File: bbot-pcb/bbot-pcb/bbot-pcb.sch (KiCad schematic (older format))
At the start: 9 parts, among them U1 HA-552-4P, U10 L293D, U2 HMC5883L, U3 HA-552-4P, U4 ArduinoProMicro, U5 L7805, U6 Screw_Terminal_2, U7 74HC595, U9 L293D

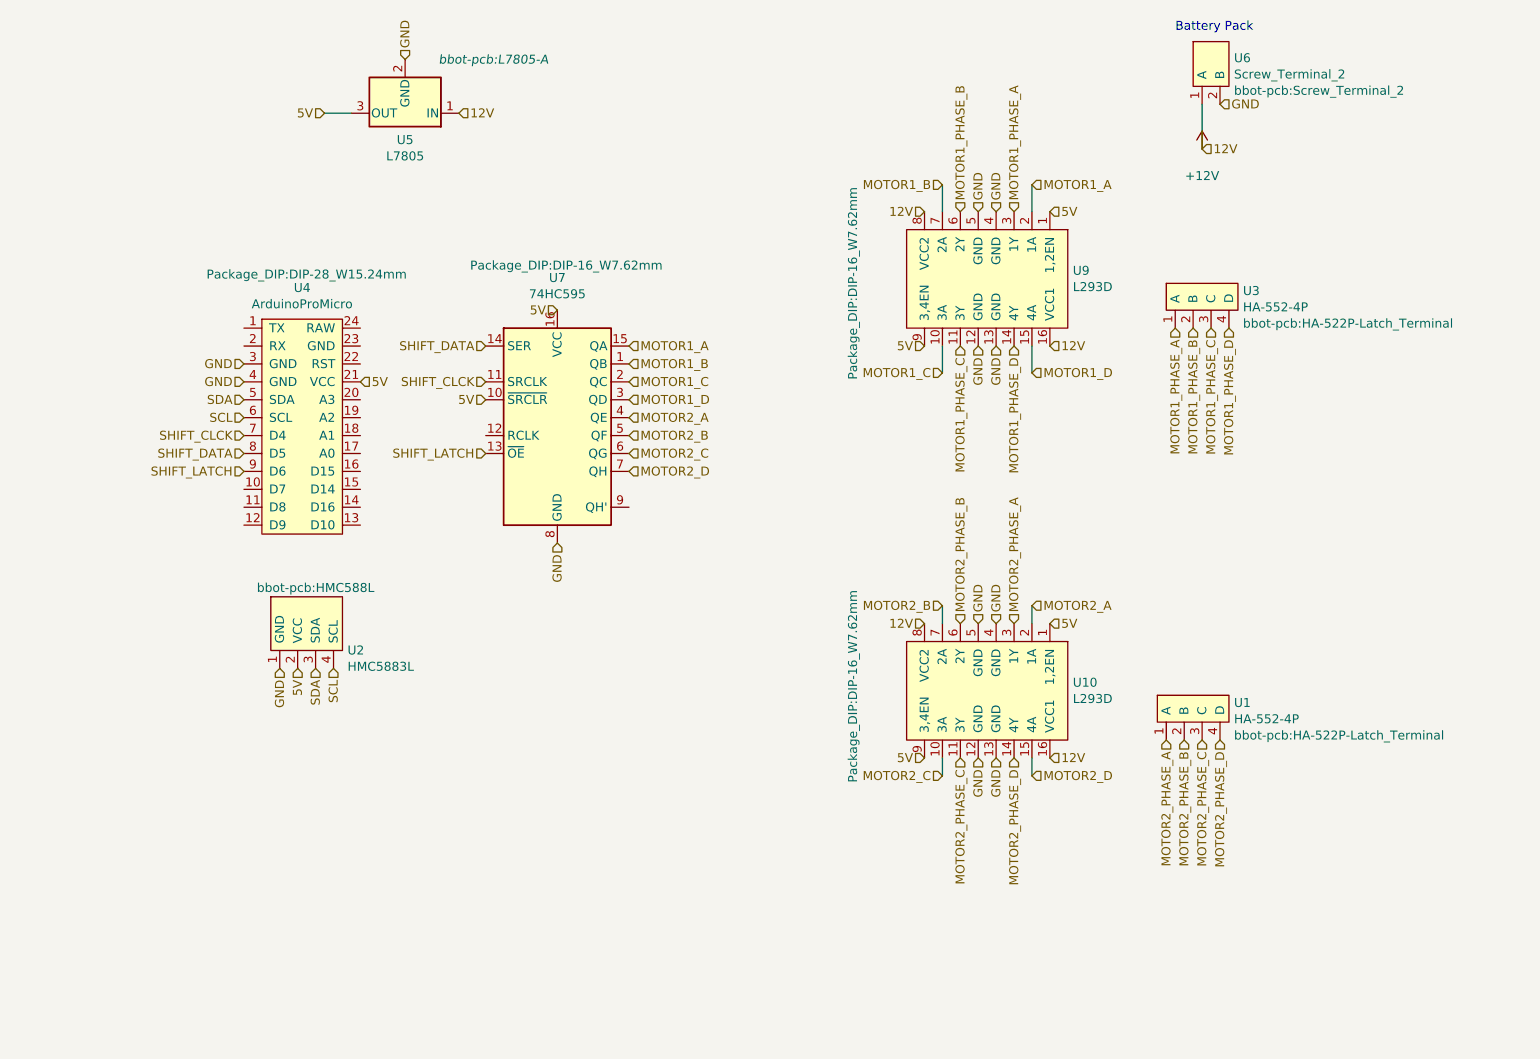
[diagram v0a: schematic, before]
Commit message: unverified prototype of completed circuit board design. not quite ready to ship off to a fab yet
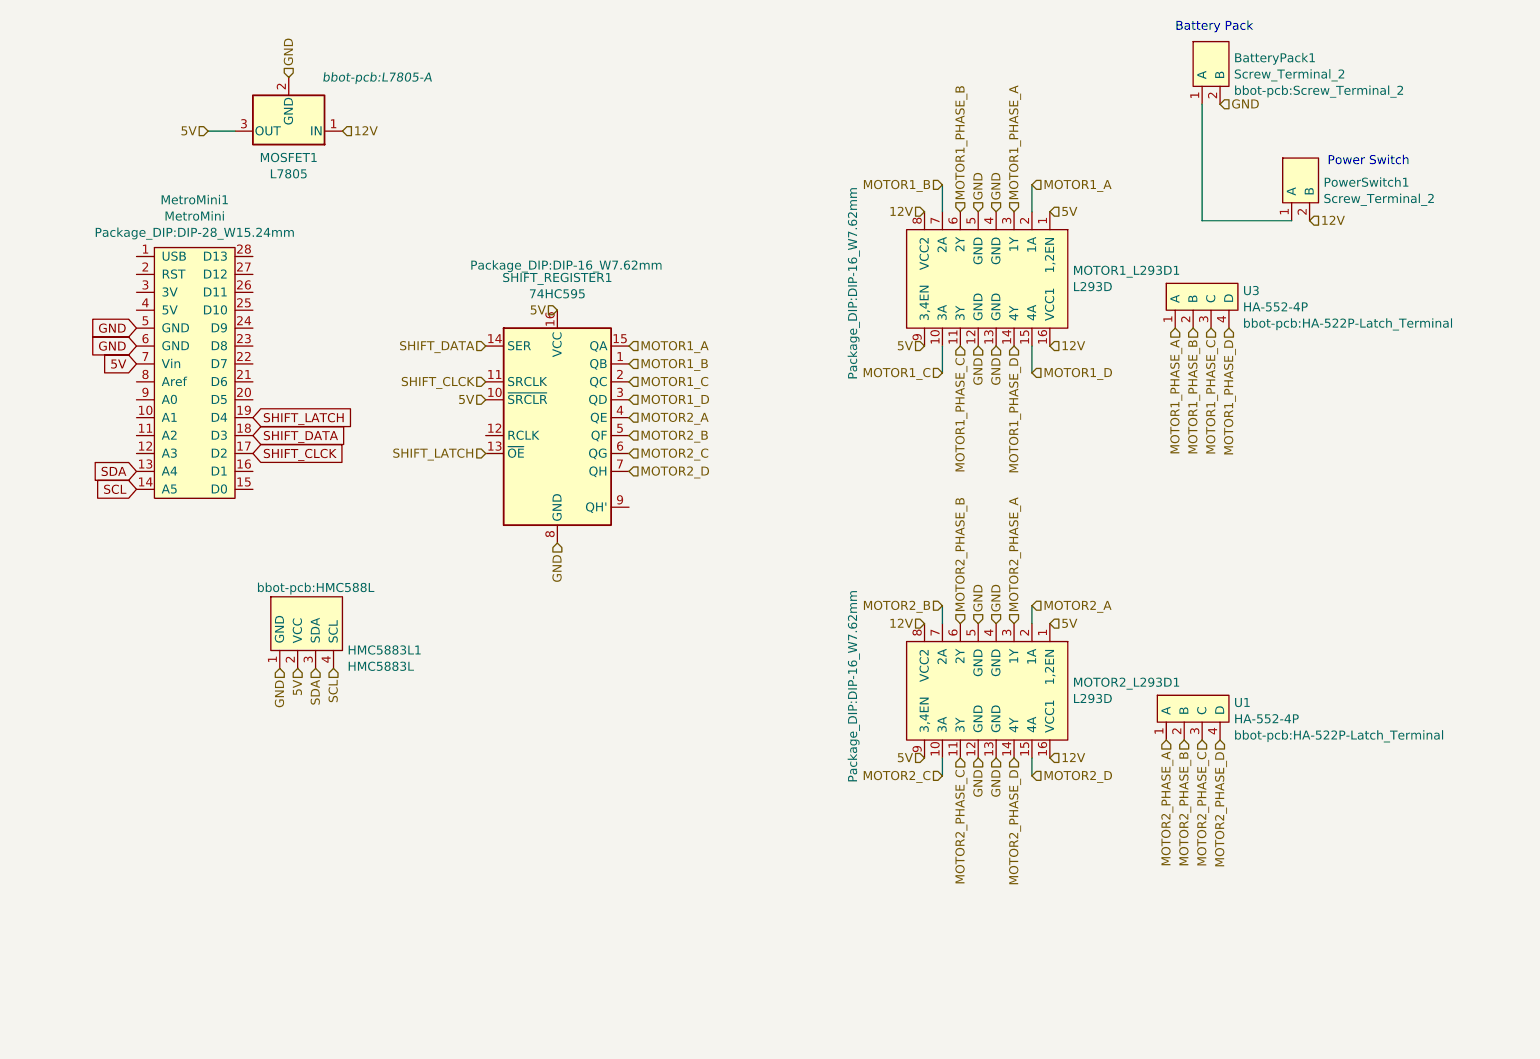
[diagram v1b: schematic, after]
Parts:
- removed U4: ArduinoProMicro, Package_DIP:DIP-28_W15.24mm, symbol bbot-component-library:ArduinoProMicro
- added MetroMini1: MetroMini, Package_DIP:DIP-28_W15.24mm, symbol bbot-component-library:MetroMini
- added PowerSwitch1: Screw_Terminal_2, bbot-pcb:Screw_Terminal_2, symbol bbot-component-library:Screw_Terminal_2
- renumbered U6 to BatteryPack1, U2 to HMC5883L1, U5 to MOSFET1, U9 to MOTOR1_L293D1, U10 to MOTOR2_L293D1, U7 to SHIFT_REGISTER1
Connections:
- net 5V: now also MetroMini1.7 (Vin)
- net GND: now also MetroMini1.5 (GND), MetroMini1.6 (GND)
- net SCL: now also MetroMini1.14 (A5)
- net SDA: now also MetroMini1.13 (A4)
- net SHIFT_CLCK: now also MetroMini1.17 (D2)
- net SHIFT_DATA: now also MetroMini1.18 (D3)
- net SHIFT_LATCH: now also MetroMini1.19 (D4)
- net +12V renamed 12V
- net 12V: now also PowerSwitch1.2 (B); no longer BatteryPack1.1 (A)
- new net: BatteryPack1.1 (A), PowerSwitch1.1 (A)
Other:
- note added: "Power Switch"
- moved on the sheet: MOSFET1
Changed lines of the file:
@@
 $EndDescr
 $Comp
-L bbot-component-library:L293D U9
+L bbot-component-library:L293D MOTOR1_L293D1
 U 1 1 606C2560
 P 5950 2000
-F 0 "U9" V 5879 2478 50  0000 L CNN
+F 0 "MOTOR1_L293D1" V 5879 2478 50  0000 L CNN
 F 1 "L293D" V 5970 2478 50  0000 L CNN
 F 2 "Package_DIP:DIP-16_W7.62mm" H 5950 1250 50  0000 C CNN
@@
 $EndComp
 $Comp
-L Regulator_Linear:L7805 U5
-U 1 1 606D0E09
-P 2700 1050
-F 0 "U5" H 2700 1199 50  0000 C CNN
-F 1 "L7805" H 2700 1290 50  0000 C CNN
-F 2 "bbot-pcb:L7805-A" H 1900 750 50  0000 L CIN
-F 3 "http://www.st.com/content/ccc/resource/technical/document/datasheet/41/4f/b3/b0/12/d4/47/88/CD00000444.pdf/files/CD00000444.pdf/jcr:content/translations/en.CD00000444.pdf" H 2700 1000 50  0001 C CNN
-	1    2700 1050
-	-1   0    0    1
-$EndComp
-$Comp
-L bbot-component-library:ArduinoProMicro U4
-U 1 1 606D85DE
-P 2200 2750
-F 0 "U4" H 2125 3475 50  0000 C CNN
-F 1 "ArduinoProMicro" H 2125 3384 50  0000 C CNN
-F 2 "Package_DIP:DIP-28_W15.24mm" H 2150 3550 50  0000 C CNN
-F 3 "" H 1900 3550 50  0001 C CNN
-	1    2200 2750
-	1    0    0    -1
-$EndComp
-$Comp
-L power:+12V #PWR0101
-U 1 1 606DFC80
-P 7150 1250
-F 0 "#PWR0101" H 7150 1100 50  0001 C CNN
-F 1 "+12V" H 7150 1100 50  0000 C CNN
-F 2 "" H 7150 1250 50  0001 C CNN
-F 3 "" H 7150 1250 50  0001 C CNN
-	1    7150 1250
-	1    0    0    -1
-$EndComp
-$Comp
-L 74xx:74HC595 U7
+L 74xx:74HC595 SHIFT_REGISTER1
 U 1 1 606C82E5
 P 3550 2750
-F 0 "U7" H 3550 3531 50  0000 C CNN
+F 0 "SHIFT_REGISTER1" H 3550 3531 50  0000 C CNN
 F 1 "74HC595" H 3550 3440 50  0000 C CNN
 F 2 "Package_DIP:DIP-16_W7.62mm" H 3600 3600 50  0000 C CNN
@@
 Text HLabel 2000 4150 3    50   Input ~ 0
 GND
-Text HLabel 1800 2450 0    50   Input ~ 0
-GND
-Text HLabel 1800 2550 0    50   Input ~ 0
-GND
-Text HLabel 2700 750  1    50   Input ~ 0
-GND
-Text HLabel 7150 1250 2    50   Input ~ 0
-12V
-Text HLabel 3000 1050 2    50   Input ~ 0
+Text HLabel 2050 850  1    50   Input ~ 0
+GND
+Text HLabel 2350 1150 2    50   Input ~ 0
 12V
 Text HLabel 6300 2350 2    50   Input ~ 0
@@
 12V
 Wire Wire Line
-	2400 1050 2250 1050
-Text HLabel 2250 1050 0    50   Input ~ 0
-5V
-Text HLabel 2450 2550 2    50   Input ~ 0
+	1750 1150 1600 1150
+Text HLabel 1600 1150 0    50   Input ~ 0
 5V
 Text HLabel 3550 2150 0    50   Input ~ 0
@@
 SDA
 Text HLabel 2300 4150 3    50   Input ~ 0
-SCL
-Text HLabel 1800 2650 0    50   Input ~ 0
-SDA
-Text HLabel 1800 2750 0    50   Input ~ 0
 SCL
 Text HLabel 6100 1600 1    50   Input ~ 0
@@
 MOTOR1_PHASE_D
 $Comp
-L bbot-component-library:L293D U10
+L bbot-component-library:L293D MOTOR2_L293D1
 U 1 1 606C1081
 P 5950 4300
-F 0 "U10" V 5879 4778 50  0000 L CNN
+F 0 "MOTOR2_L293D1" V 5879 4778 50  0000 L CNN
 F 1 "L293D" V 5970 4778 50  0000 L CNN
 F 2 "Package_DIP:DIP-16_W7.62mm" H 5900 3550 50  0000 C CNN
@@
 Text HLabel 3150 2350 0    50   Input ~ 0
 SHIFT_DATA
-Text HLabel 1800 2850 0    50   Input ~ 0
-SHIFT_CLCK
-Text HLabel 1800 2950 0    50   Input ~ 0
-SHIFT_DATA
-Text HLabel 1800 3050 0    50   Input ~ 0
-SHIFT_LATCH
 $Comp
 L bbot-component-library:HA-552-4P U1
@@
 MOTOR2_PHASE_A
 $Comp
-L bbot-component-library:HMC5883L U2
+L bbot-component-library:HMC5883L HMC5883L1
 U 1 1 606D2B12
 P 2150 4000
-F 0 "U2" H 2378 3951 50  0000 L CNN
+F 0 "HMC5883L1" H 2378 3951 50  0000 L CNN
 F 1 "HMC5883L" H 2378 3860 50  0000 L CNN
 F 2 "bbot-pcb:HMC588L" H 2200 4300 50  0000 C CNN
@@
 $EndComp
 $Comp
-L bbot-component-library:Screw_Terminal_2 U6
+L bbot-component-library:Screw_Terminal_2 BatteryPack1
 U 1 1 607194F6
 P 7150 1000
-F 0 "U6" H 7328 1258 50  0000 L CNN
+F 0 "BatteryPack1" H 7328 1258 50  0000 L CNN
 F 1 "Screw_Terminal_2" H 7328 1167 50  0000 L CNN
 F 2 "bbot-pcb:Screw_Terminal_2" H 7328 1076 50  0000 L CNN
@@
 Text Notes 7000 600  0    50   ~ 0
 Battery Pack
-Wire Wire Line
-	7150 1250 7150 1000
 Text HLabel 7250 1000 2    50   Input ~ 0
 GND
+$Comp
+L Regulator_Linear:L7805 MOSFET1
+U 1 1 606D0E09
+P 2050 1150
+F 0 "MOSFET1" H 2050 1299 50  0000 C CNN
+F 1 "L7805" H 2050 1390 50  0000 C CNN
+F 2 "bbot-pcb:L7805-A" H 1250 850 50  0000 L CIN
+F 3 "http://www.st.com/content/ccc/resource/technical/document/datasheet/41/4f/b3/b0/12/d4/47/88/CD00000444.pdf/files/CD00000444.pdf/jcr:content/translations/en.CD00000444.pdf" H 2050 1100 50  0001 C CNN
+	1    2050 1150
+	-1   0    0    1
+$EndComp
+$Comp
+L bbot-component-library:Screw_Terminal_2 PowerSwitch1
+U 1 1 60720FFC
+P 7650 1650
+F 0 "PowerSwitch1" H 7828 1863 50  0000 L CNN
+F 1 "Screw_Terminal_2" H 7828 1772 50  0000 L CNN
+F 2 "bbot-pcb:Screw_Terminal_2" H 7650 1650 50  0001 C CNN
+F 3 "" H 7650 1650 50  0001 C CNN
+	1    7650 1650
+	1    0    0    -1
+$EndComp
+Text HLabel 7750 1650 2    50   Input ~ 0
+12V
+Text Notes 7850 1350 0    50   ~ 0
+Power Switch
+Wire Wire Line
+	7150 1000 7150 1650
+Wire Wire Line
+	7150 1650 7650 1650
+$Comp
+L bbot-component-library:MetroMini MetroMini1
+U 1 1 6072CA85
+P 1550 2500
+F 0 "MetroMini1" H 1525 3465 50  0000 C CNN
+F 1 "MetroMini" H 1525 3374 50  0000 C CNN
+F 2 "Package_DIP:DIP-28_W15.24mm" H 1525 3283 50  0000 C CNN
+F 3 "" H 1300 2850 50  0001 C CNN
+	1    1550 2500
+	1    0    0    -1
+$EndComp
+Text GLabel 1200 2450 0    50   Input ~ 0
+5V
+Text GLabel 1850 2950 2    50   Input ~ 0
+SHIFT_CLCK
+Text GLabel 1850 2850 2    50   Input ~ 0
+SHIFT_DATA
+Text GLabel 1850 2750 2    50   Input ~ 0
+SHIFT_LATCH
+Text GLabel 1200 2250 0    50   Input ~ 0
+GND
+Text GLabel 1200 2350 0    50   Input ~ 0
+GND
+Text GLabel 1200 3050 0    50   Input ~ 0
+SDA
+Text GLabel 1200 3150 0    50   Input ~ 0
+SCL
 $EndSCHEMATC

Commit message: finalize kicad circuit board.
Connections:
- net GND: now also SHIFT_REGISTER1.13 (~OE); no longer MOTOR1_L293D1.12 (GND), MOTOR1_L293D1.13 (GND), MOTOR1_L293D1.4 (GND), MOTOR2_L293D1.13 (GND), MOTOR2_L293D1.4 (GND), MOTOR2_L293D1.5 (GND)
- net SHIFT_LATCH: now also SHIFT_REGISTER1.12 (RCLK); no longer SHIFT_REGISTER1.13 (~OE)
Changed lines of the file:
@@
 Wire Wire Line
 	5700 1600 5700 1450
-Wire Wire Line
-	5700 2350 5700 2500
-Wire Wire Line
-	6200 2350 6200 2500
 Text HLabel 5700 2500 0    50   Input ~ 0
 MOTOR1_C
@@
 Text HLabel 3950 3050 2    50   Input ~ 0
 MOTOR2_D
-Text HLabel 5900 3900 1    50   Input ~ 0
-GND
-Text HLabel 6000 3900 1    50   Input ~ 0
-GND
 Text HLabel 5900 4650 3    50   Input ~ 0
 GND
-Text HLabel 6000 4650 3    50   Input ~ 0
-GND
-Text HLabel 6000 2350 3    50   Input ~ 0
-GND
-Text HLabel 5900 2350 3    50   Input ~ 0
-GND
 Text HLabel 5900 1600 1    50   Input ~ 0
-GND
-Text HLabel 6000 1600 1    50   Input ~ 0
 GND
 Text HLabel 3550 3450 3    50   Input ~ 0
@@
 5V
 Text HLabel 3150 2950 0    50   Input ~ 0
-SHIFT_LATCH
+GND
 Text HLabel 3150 2350 0    50   Input ~ 0
 SHIFT_DATA
@@
 Text GLabel 1200 3150 0    50   Input ~ 0
 SCL
+Wire Wire Line
+	5700 2350 5700 2500
+Wire Wire Line
+	6200 2350 6200 2500
+Text HLabel 3150 2850 0    50   Input ~ 0
+SHIFT_LATCH
 $EndSCHEMATC

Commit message: pcb v2 updates
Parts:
- removed HMC5883L1: HMC5883L, bbot-pcb:HMC588L, symbol bbot-component-library:HMC5883L
- added U2: ADXL335, bbot-pcb:ADXL335, symbol bbot-component-library:ADXL335
- added U4: OPENLOG, bbot-pcb:OPENLOG, symbol bbot-component-library:OPENLOG
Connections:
- net GND: now also U2.5 (GND), U4.1 (BLK), U4.2 (GND)
- net A1: now reaches MetroMini1.10 (A1)
- net A1: now also U2.3 (YOUT)
- net A2: now reaches MetroMini1.11 (A2)
- net A2: now also U2.4 (ZOUT)
- net RST: now reaches MetroMini1.2 (RST)
- net RST: now also U4.6 (GRN)
- net RX: now reaches MetroMini1.24 (D9)
- net RX: now also U4.5 (RX1)
- net TX: now reaches MetroMini1.25 (D10)
- net TX: now also U4.4 (TX0)
- net 3V: now reaches MetroMini1.3 (3V)
- net 3V: now also U2.1 (VCC), U4.3 (VCC)
- net A0: now reaches MetroMini1.9 (A0)
- net A0: now also U2.2 (XOUT)
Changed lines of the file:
@@
 Text HLabel 3550 3450 3    50   Input ~ 0
-GND
-Text HLabel 2000 4150 3    50   Input ~ 0
 GND
 Text HLabel 2050 850  1    50   Input ~ 0
@@
 Text HLabel 3550 2150 0    50   Input ~ 0
 5V
-Text HLabel 2100 4150 3    50   Input ~ 0
-5V
-Text HLabel 2200 4150 3    50   Input ~ 0
-SDA
-Text HLabel 2300 4150 3    50   Input ~ 0
-SCL
 Text HLabel 6100 1600 1    50   Input ~ 0
 MOTOR1_PHASE_A
@@
 MOTOR2_PHASE_A
 $Comp
-L bbot-component-library:HMC5883L HMC5883L1
-U 1 1 606D2B12
-P 2150 4000
-F 0 "HMC5883L1" H 2378 3951 50  0000 L CNN
-F 1 "HMC5883L" H 2378 3860 50  0000 L CNN
-F 2 "bbot-pcb:HMC588L" H 2200 4300 50  0000 C CNN
-F 3 "" H 2200 4200 50  0001 C CNN
-	1    2150 4000
-	1    0    0    -1
-$EndComp
-$Comp
 L bbot-component-library:Screw_Terminal_2 BatteryPack1
 U 1 1 607194F6
@@
 Text HLabel 3150 2850 0    50   Input ~ 0
 SHIFT_LATCH
+$Comp
+L bbot-component-library:ADXL335 U2
+U 1 1 607BD863
+P 1500 3950
+F 0 "U2" H 1778 3846 50  0000 L CNN
+F 1 "ADXL335" H 1778 3755 50  0000 L CNN
+F 2 "bbot-pcb:ADXL335" H 1550 4150 50  0000 C CNN
+F 3 "" H 1250 4000 50  0001 C CNN
+	1    1500 3950
+	1    0    0    -1
+$EndComp
+Text HLabel 1250 3900 0    50   Input ~ 0
+3V
+Text HLabel 1250 4000 0    50   Input ~ 0
+A0
+Text HLabel 1250 4100 0    50   Input ~ 0
+A1
+Text HLabel 1250 4200 0    50   Input ~ 0
+A2
+Text HLabel 1250 4300 0    50   Input ~ 0
+GND
+Text HLabel 1200 2650 0    50   Input ~ 0
+A0
+Text HLabel 1200 2750 0    50   Input ~ 0
+A1
+Text HLabel 1200 2850 0    50   Input ~ 0
+A2
+Text HLabel 1200 2050 0    50   Input ~ 0
+3V
+$Comp
+L bbot-component-library:OPENLOG U4
+U 1 1 607C091B
+P 3550 4050
+F 0 "U4" H 3828 4096 50  0000 L CNN
+F 1 "OPENLOG" H 3828 4005 50  0000 L CNN
+F 2 "bbot-pcb:OPENLOG" H 3828 3914 50  0000 L CNN
+F 3 "" H 3250 4250 50  0001 C CNN
+	1    3550 4050
+	1    0    0    -1
+$EndComp
+Text HLabel 3250 4050 0    50   Input ~ 0
+3V
+Text HLabel 3250 3950 0    50   Input ~ 0
+GND
+Text HLabel 3250 3850 0    50   Input ~ 0
+GND
+Text HLabel 3250 4150 0    50   Input ~ 0
+TX
+Text HLabel 3250 4250 0    50   Input ~ 0
+RX
+Text HLabel 1850 2150 2    50   Input ~ 0
+TX
+Text HLabel 1850 2250 2    50   Input ~ 0
+RX
+Text HLabel 3250 4350 0    50   Input ~ 0
+RST
+Text HLabel 1200 1950 0    50   Input ~ 0
+RST
 $EndSCHEMATC
